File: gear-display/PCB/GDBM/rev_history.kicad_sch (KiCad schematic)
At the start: 0 parts

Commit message: rikki
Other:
- company: (none) -> Kallio Designs Oy
- title: (none) -> Gear Display Board
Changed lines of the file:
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@@
 (kicad_sch (version 20211123) (generator eeschema)
   (paper "A4")
+  (title_block
+    (title "Gear Display Board")
+    (date "2022-08-13")
+    (rev "1.0")
+    (company "Kallio Designs Oy")
+    (comment 1 "Teemu Latonen")
+    (comment 2 "000064")
+    (comment 3 "000065")
+  )
   (polyline (pts (xy 57.15 48.26) (xy 57.15 53.34))
     (stroke (width 0) (type solid) (color 0 0 0 1))

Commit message: documentation
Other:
- note added: "01.03.2023"
- note added: "2.0"
- note added: "Buffer U8 added for LED strip"
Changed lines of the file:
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@@
     (comment 3 "000065")
+  )
+  (polyline (pts (xy 57.15 66.04) (xy 243.84 66.04))
+    (stroke (width 0) (type solid) (color 0 0 0 1))
   )
   (polyline (pts (xy 57.15 48.26) (xy 57.15 53.34))
@@
     (stroke (width 0) (type solid) (color 0 0 0 1))
   )
+  (text "2.0" (at 58.42 64.77 0)
+    (effects (font (size 2 2)) (justify left bottom))
+  )
   (text "13.08.2022" (at 69.85 58.42 0)
     (effects (font (size 2 2)) (justify left bottom))
@@
   (text "DESCRIPTION" (at 90.17 53.34 0)
     (effects (font (size 2 2) (thickness 1) bold) (justify left bottom))
+  )
+  (text "01.03.2023" (at 69.85 64.77 0)
+    (effects (font (size 2 2)) (justify left bottom))
+  )
+  (text "Teemu Latonen" (at 208.28 64.77 0)
+    (effects (font (size 2 2)) (justify left bottom))
   )
   (text "REVISION HISTORY" (at 58.42 48.26 0)
@@
     (effects (font (size 2 2)) (justify left bottom))
   )
+  (text "Buffer U8 added for LED strip" (at 90.17 64.77 0)
+    (effects (font (size 2 2)) (justify left bottom))
+  )

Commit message: Documentation update
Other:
- note added: "27.03.2023"
- note added: "3.0"
- note added: "7-segment display configuration changed"
- note added: "External dimmer circuit added"
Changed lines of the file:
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@@
     (comment 3 "000065")
+  )
+  (polyline (pts (xy 57.15 72.39) (xy 243.84 72.39))
+    (stroke (width 0) (type solid) (color 0 0 0 1))
   )
   (polyline (pts (xy 57.15 66.04) (xy 243.84 66.04))
@@
   )
   (polyline (pts (xy 57.15 48.26) (xy 57.15 53.34))
+    (stroke (width 0) (type solid) (color 0 0 0 1))
+  )
+  (polyline (pts (xy 57.15 78.74) (xy 243.84 78.74))
     (stroke (width 0) (type solid) (color 0 0 0 1))
   )
@@
   )
   (polyline (pts (xy 57.15 53.34) (xy 243.84 53.34))
+    (stroke (width 0) (type solid) (color 0 0 0 1))
+  )
+  (polyline (pts (xy 57.15 85.09) (xy 243.84 85.09))
     (stroke (width 0) (type solid) (color 0 0 0 1))
   )
@@
     (stroke (width 0) (type solid) (color 0 0 0 1))
   )
+  (text "3.0" (at 58.42 83.82 0)
+    (effects (font (size 2 2)) (justify left bottom))
+  )
   (text "2.0" (at 58.42 64.77 0)
     (effects (font (size 2 2)) (justify left bottom))
@@
   (text "DESCRIPTION" (at 90.17 53.34 0)
     (effects (font (size 2 2) (thickness 1) bold) (justify left bottom))
+  )
+  (text "External dimmer circuit added" (at 90.17 77.47 0)
+    (effects (font (size 2 2)) (justify left bottom))
+  )
+  (text "7-segment display configuration changed" (at 90.17 83.82 0)
+    (effects (font (size 2 2)) (justify left bottom))
   )
   (text "01.03.2023" (at 69.85 64.77 0)
@@
     (effects (font (size 2 2) (thickness 1) bold) (justify left bottom))
   )
+  (text "Teemu Latonen" (at 208.28 71.12 0)
+    (effects (font (size 2 2)) (justify left bottom))
+  )
+  (text "Teemu Latonen" (at 208.28 77.47 0)
+    (effects (font (size 2 2)) (justify left bottom))
+  )
   (text "DATE" (at 69.85 53.34 0)
     (effects (font (size 2 2) (thickness 1) bold) (justify left bottom))
   )
+  (text "7-segment display configuration changed" (at 90.17 71.12 0)
+    (effects (font (size 2 2)) (justify left bottom))
+  )
   (text "1.0" (at 58.42 58.42 0)
+    (effects (font (size 2 2)) (justify left bottom))
+  )
+  (text "Teemu Latonen" (at 208.28 83.82 0)
     (effects (font (size 2 2)) (justify left bottom))
   )
@@
     (effects (font (size 2 2)) (justify left bottom))
   )
+  (text "27.03.2023" (at 69.85 83.82 0)
+    (effects (font (size 2 2)) (justify left bottom))
+  )

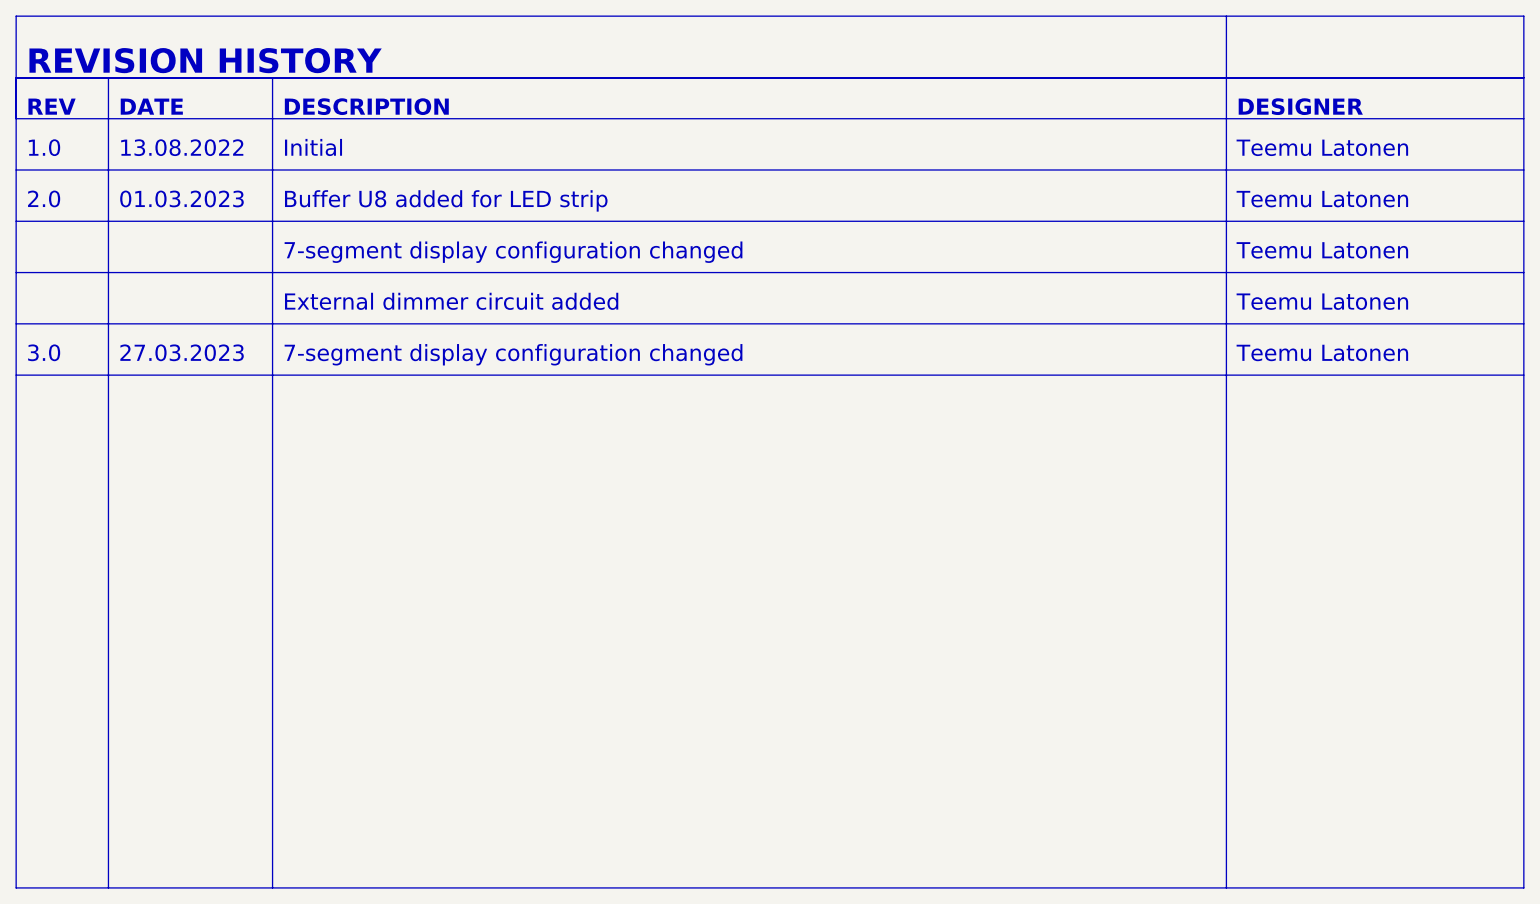
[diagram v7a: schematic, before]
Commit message: R33 value change
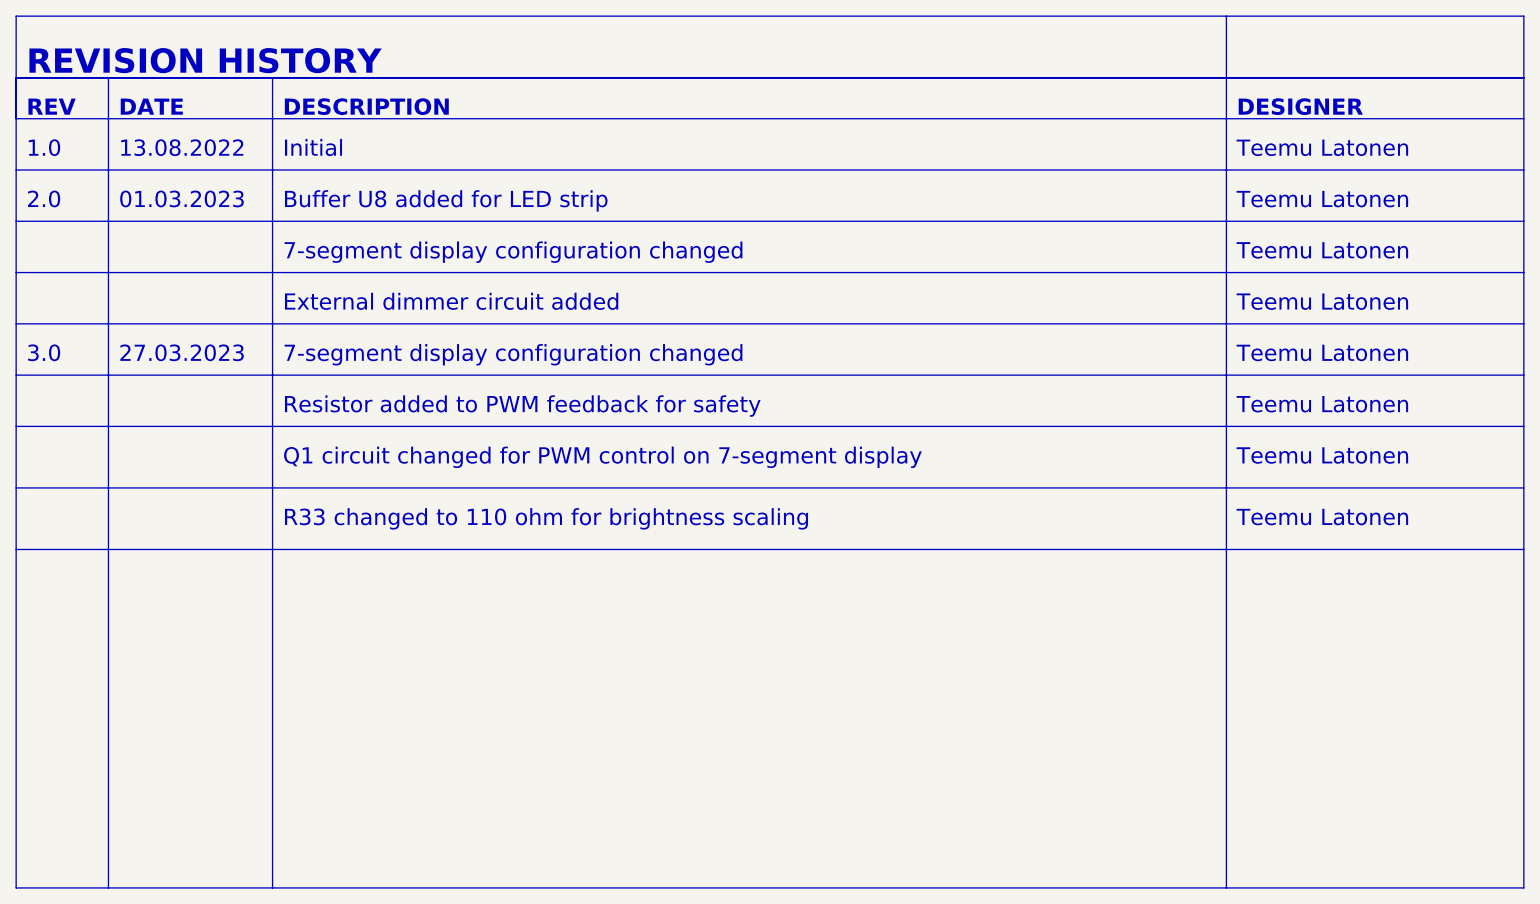
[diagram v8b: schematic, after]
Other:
- note added: "Q1 circuit changed for PWM control on 7-segment display"
- note added: "R33 changed to 110 ohm for brightness scaling"
- note added: "Resistor added to PWM feedback for safety"
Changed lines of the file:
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@@
+    (stroke (width 0) (type solid) (color 0 0 0 1))
+  )
+  (polyline (pts (xy 57.15 91.44) (xy 243.84 91.44))
     (stroke (width 0) (type solid) (color 0 0 0 1))
   )
@@
   )
   (polyline (pts (xy 57.15 48.26) (xy 57.15 148.59))
+    (stroke (width 0) (type solid) (color 0 0 0 1))
+  )
+  (polyline (pts (xy 57.15 99.06) (xy 243.84 99.06))
     (stroke (width 0) (type solid) (color 0 0 0 1))
   )
@@
     (stroke (width 0) (type solid) (color 0 0 0 1))
   )
+  (polyline (pts (xy 57.15 106.68) (xy 243.84 106.68))
+    (stroke (width 0) (type solid) (color 0 0 0 1))
+  )
   (polyline (pts (xy 57.15 40.64) (xy 57.15 48.26))
     (stroke (width 0) (type solid) (color 0 0 0 1))
@@
   )
   (text "13.08.2022" (at 69.85 58.42 0)
+    (effects (font (size 2 2)) (justify left bottom))
+  )
+  (text "Resistor added to PWM feedback for safety" (at 90.17 90.17 0)
     (effects (font (size 2 2)) (justify left bottom))
   )
@@
     (effects (font (size 2 2)) (justify left bottom))
   )
+  (text "Teemu Latonen" (at 208.28 96.52 0)
+    (effects (font (size 2 2)) (justify left bottom))
+  )
   (text "REVISION HISTORY" (at 58.42 48.26 0)
     (effects (font (size 3 3) (thickness 1) bold) (justify left bottom))
   )
+  (text "R33 changed to 110 ohm for brightness scaling" (at 90.17 104.14 0)
+    (effects (font (size 2 2)) (justify left bottom))
+  )
   (text "DESIGNER" (at 208.28 53.34 0)
     (effects (font (size 2 2) (thickness 1) bold) (justify left bottom))
+  )
+  (text "Teemu Latonen" (at 208.28 90.17 0)
+    (effects (font (size 2 2)) (justify left bottom))
   )
   (text "Teemu Latonen" (at 208.28 71.12 0)
@@
     (effects (font (size 2 2)) (justify left bottom))
   )
+  (text "Teemu Latonen" (at 208.28 104.14 0)
+    (effects (font (size 2 2)) (justify left bottom))
+  )
   (text "Initial" (at 90.17 58.42 0)
     (effects (font (size 2 2)) (justify left bottom))
@@
     (effects (font (size 2 2)) (justify left bottom))
   )
+  (text "Q1 circuit changed for PWM control on 7-segment display"
+    (at 90.17 96.52 0)
+    (effects (font (size 2 2)) (justify left bottom))
+  )
